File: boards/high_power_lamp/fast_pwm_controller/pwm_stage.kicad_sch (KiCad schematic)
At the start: 8 parts, among them Q1 BUK7516-55A,127, U1 4050

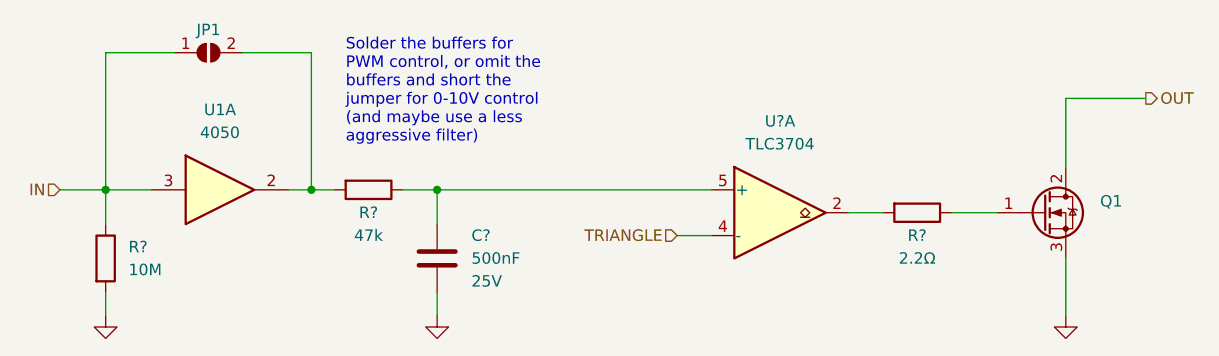
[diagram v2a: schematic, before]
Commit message: almost finish arranging the fast pwm controller pcb
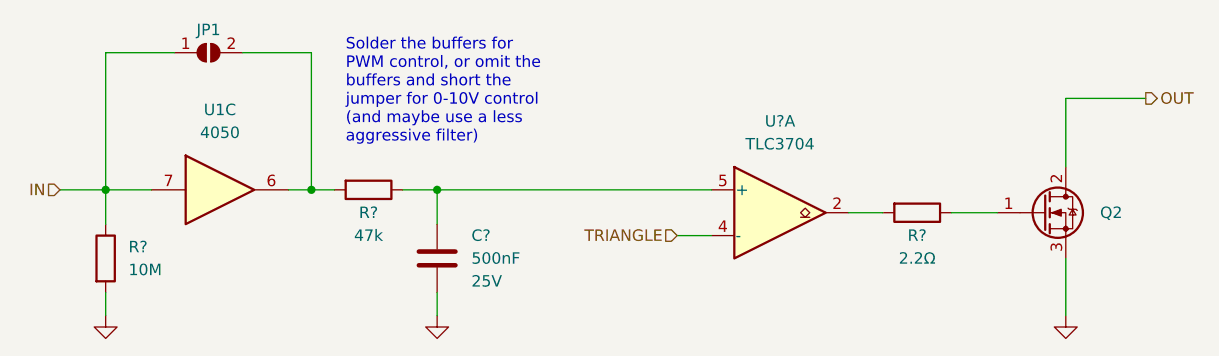
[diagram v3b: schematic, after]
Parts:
- renumbered Q1 to Q2
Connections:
- net IN: now also U1.7; no longer U1.3
- net at JP1.2 (B), R?.2: now also U1.6; no longer U1.2
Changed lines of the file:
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@@
         )
         (path "/ebb02bb0-15d4-41b5-b7b0-053d51d38d86/1dc02105-34f4-4dcd-909a-a43f3cf6326e"
+          (reference "R20") (unit 1)
+        )
+        (path "/ebb02bb0-15d4-41b5-b7b0-053d51d38d86/7bb7f3cd-bd16-48a2-9709-ee0db83f3451"
           (reference "R13") (unit 1)
-        )
-        (path "/ebb02bb0-15d4-41b5-b7b0-053d51d38d86/7bb7f3cd-bd16-48a2-9709-ee0db83f3451"
-          (reference "R20") (unit 1)
         )
         (path "/ebb02bb0-15d4-41b5-b7b0-053d51d38d86/abcbc788-820f-4167-8f5b-0037e0acabb5"
@@
     )
   )
-  (symbol (lib_id "4xxx:4050") (at 95.25 81.28 0) (unit 1)
+  (symbol (lib_id "4xxx:4050") (at 95.25 81.28 0) (unit 3)
     (in_bom yes) (on_board yes) (dnp no) (fields_autoplaced)
     (property "Reference" "U1" (at 95.25 72.39 0)
@@
       (project "fast_pwm_controller"
         (path "/ebb02bb0-15d4-41b5-b7b0-053d51d38d86/1dc02105-34f4-4dcd-909a-a43f3cf6326e"
+          (reference "U1") (unit 3)
+        )
+        (path "/ebb02bb0-15d4-41b5-b7b0-053d51d38d86/7bb7f3cd-bd16-48a2-9709-ee0db83f3451"
           (reference "U1") (unit 1)
         )
-        (path "/ebb02bb0-15d4-41b5-b7b0-053d51d38d86/7bb7f3cd-bd16-48a2-9709-ee0db83f3451"
+        (path "/ebb02bb0-15d4-41b5-b7b0-053d51d38d86/abcbc788-820f-4167-8f5b-0037e0acabb5"
+          (reference "U1") (unit 4)
+        )
+        (path "/ebb02bb0-15d4-41b5-b7b0-053d51d38d86/7c02a172-be14-404a-b556-b25540aed647"
           (reference "U1") (unit 2)
-        )
-        (path "/ebb02bb0-15d4-41b5-b7b0-053d51d38d86/abcbc788-820f-4167-8f5b-0037e0acabb5"
-          (reference "U1") (unit 3)
-        )
-        (path "/ebb02bb0-15d4-41b5-b7b0-053d51d38d86/7c02a172-be14-404a-b556-b25540aed647"
-          (reference "U1") (unit 4)
         )
       )
@@
   (symbol (lib_id "Device:Q_NMOS_GDS") (at 186.69 83.82 0) (unit 1)
     (in_bom yes) (on_board yes) (dnp no) (fields_autoplaced)
-    (property "Reference" "Q1" (at 193.04 82.55 0)
+    (property "Reference" "Q2" (at 193.04 83.82 0)
       (effects (font (size 1.27 1.27)) (justify left))
     )
@@
       (project "fast_pwm_controller"
         (path "/ebb02bb0-15d4-41b5-b7b0-053d51d38d86/1dc02105-34f4-4dcd-909a-a43f3cf6326e"
+          (reference "Q2") (unit 1)
+        )
+        (path "/ebb02bb0-15d4-41b5-b7b0-053d51d38d86/7bb7f3cd-bd16-48a2-9709-ee0db83f3451"
           (reference "Q1") (unit 1)
         )
-        (path "/ebb02bb0-15d4-41b5-b7b0-053d51d38d86/7bb7f3cd-bd16-48a2-9709-ee0db83f3451"
-          (reference "Q2") (unit 1)
-        )
-        (path "/ebb02bb0-15d4-41b5-b7b0-053d51d38d86/abcbc788-820f-4167-8f5b-0037e0acabb5"
+        (path "/ebb02bb0-15d4-41b5-b7b0-053d51d38d86/abcbc788-820f-4167-8f5b-0037e0acabb5"

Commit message: prepare traces
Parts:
- renumbered Q2 to Q1
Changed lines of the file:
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@@
         )
         (path "/ebb02bb0-15d4-41b5-b7b0-053d51d38d86/1dc02105-34f4-4dcd-909a-a43f3cf6326e"
-          (reference "#PWR034") (unit 1)
-        )
-        (path "/ebb02bb0-15d4-41b5-b7b0-053d51d38d86/7bb7f3cd-bd16-48a2-9709-ee0db83f3451"
-          (reference "#PWR047") (unit 1)
-        )
-        (path "/ebb02bb0-15d4-41b5-b7b0-053d51d38d86/abcbc788-820f-4167-8f5b-0037e0acabb5"
-          (reference "#PWR050") (unit 1)
-        )
-        (path "/ebb02bb0-15d4-41b5-b7b0-053d51d38d86/7c02a172-be14-404a-b556-b25540aed647"
-          (reference "#PWR053") (unit 1)
+          (reference "#PWR035") (unit 1)
+        )
+        (path "/ebb02bb0-15d4-41b5-b7b0-053d51d38d86/7bb7f3cd-bd16-48a2-9709-ee0db83f3451"
+          (reference "#PWR048") (unit 1)
+        )
+        (path "/ebb02bb0-15d4-41b5-b7b0-053d51d38d86/abcbc788-820f-4167-8f5b-0037e0acabb5"
+          (reference "#PWR051") (unit 1)
+        )
+        (path "/ebb02bb0-15d4-41b5-b7b0-053d51d38d86/7c02a172-be14-404a-b556-b25540aed647"
+          (reference "#PWR054") (unit 1)
         )
       )
@@
         )
         (path "/ebb02bb0-15d4-41b5-b7b0-053d51d38d86/1dc02105-34f4-4dcd-909a-a43f3cf6326e"
-          (reference "#PWR035") (unit 1)
-        )
-        (path "/ebb02bb0-15d4-41b5-b7b0-053d51d38d86/7bb7f3cd-bd16-48a2-9709-ee0db83f3451"
-          (reference "#PWR048") (unit 1)
-        )
-        (path "/ebb02bb0-15d4-41b5-b7b0-053d51d38d86/abcbc788-820f-4167-8f5b-0037e0acabb5"
-          (reference "#PWR051") (unit 1)
-        )
-        (path "/ebb02bb0-15d4-41b5-b7b0-053d51d38d86/7c02a172-be14-404a-b556-b25540aed647"
-          (reference "#PWR054") (unit 1)
+          (reference "#PWR036") (unit 1)
+        )
+        (path "/ebb02bb0-15d4-41b5-b7b0-053d51d38d86/7bb7f3cd-bd16-48a2-9709-ee0db83f3451"
+          (reference "#PWR049") (unit 1)
+        )
+        (path "/ebb02bb0-15d4-41b5-b7b0-053d51d38d86/abcbc788-820f-4167-8f5b-0037e0acabb5"
+          (reference "#PWR052") (unit 1)
+        )
+        (path "/ebb02bb0-15d4-41b5-b7b0-053d51d38d86/7c02a172-be14-404a-b556-b25540aed647"
+          (reference "#PWR055") (unit 1)
         )
       )
@@
         )
         (path "/ebb02bb0-15d4-41b5-b7b0-053d51d38d86/1dc02105-34f4-4dcd-909a-a43f3cf6326e"
+          (reference "R13") (unit 1)
+        )
+        (path "/ebb02bb0-15d4-41b5-b7b0-053d51d38d86/7bb7f3cd-bd16-48a2-9709-ee0db83f3451"
           (reference "R20") (unit 1)
-        )
-        (path "/ebb02bb0-15d4-41b5-b7b0-053d51d38d86/7bb7f3cd-bd16-48a2-9709-ee0db83f3451"
-          (reference "R13") (unit 1)
         )
         (path "/ebb02bb0-15d4-41b5-b7b0-053d51d38d86/abcbc788-820f-4167-8f5b-0037e0acabb5"
@@
         )
         (path "/ebb02bb0-15d4-41b5-b7b0-053d51d38d86/1dc02105-34f4-4dcd-909a-a43f3cf6326e"
-          (reference "#PWR036") (unit 1)
-        )
-        (path "/ebb02bb0-15d4-41b5-b7b0-053d51d38d86/7bb7f3cd-bd16-48a2-9709-ee0db83f3451"
-          (reference "#PWR049") (unit 1)
-        )
-        (path "/ebb02bb0-15d4-41b5-b7b0-053d51d38d86/abcbc788-820f-4167-8f5b-0037e0acabb5"
-          (reference "#PWR052") (unit 1)
-        )
-        (path "/ebb02bb0-15d4-41b5-b7b0-053d51d38d86/7c02a172-be14-404a-b556-b25540aed647"
-          (reference "#PWR055") (unit 1)
+          (reference "#PWR037") (unit 1)
+        )
+        (path "/ebb02bb0-15d4-41b5-b7b0-053d51d38d86/7bb7f3cd-bd16-48a2-9709-ee0db83f3451"
+          (reference "#PWR050") (unit 1)
+        )
+        (path "/ebb02bb0-15d4-41b5-b7b0-053d51d38d86/abcbc788-820f-4167-8f5b-0037e0acabb5"
+          (reference "#PWR053") (unit 1)
+        )
+        (path "/ebb02bb0-15d4-41b5-b7b0-053d51d38d86/7c02a172-be14-404a-b556-b25540aed647"
+          (reference "#PWR056") (unit 1)
         )
       )
@@
         )
         (path "/ebb02bb0-15d4-41b5-b7b0-053d51d38d86/1dc02105-34f4-4dcd-909a-a43f3cf6326e"
-          (reference "C7") (unit 1)
-        )
-        (path "/ebb02bb0-15d4-41b5-b7b0-053d51d38d86/7bb7f3cd-bd16-48a2-9709-ee0db83f3451"
-          (reference "C15") (unit 1)
-        )
-        (path "/ebb02bb0-15d4-41b5-b7b0-053d51d38d86/abcbc788-820f-4167-8f5b-0037e0acabb5"
+          (reference "C8") (unit 1)
+        )
+        (path "/ebb02bb0-15d4-41b5-b7b0-053d51d38d86/7bb7f3cd-bd16-48a2-9709-ee0db83f3451"
           (reference "C16") (unit 1)
         )
-        (path "/ebb02bb0-15d4-41b5-b7b0-053d51d38d86/7c02a172-be14-404a-b556-b25540aed647"
+        (path "/ebb02bb0-15d4-41b5-b7b0-053d51d38d86/abcbc788-820f-4167-8f5b-0037e0acabb5"
           (reference "C17") (unit 1)
+        )
+        (path "/ebb02bb0-15d4-41b5-b7b0-053d51d38d86/7c02a172-be14-404a-b556-b25540aed647"
+          (reference "C18") (unit 1)
         )
       )
@@
   (symbol (lib_id "Device:Q_NMOS_GDS") (at 186.69 83.82 0) (unit 1)
     (in_bom yes) (on_board yes) (dnp no) (fields_autoplaced)
-    (property "Reference" "Q2" (at 193.04 83.82 0)
+    (property "Reference" "Q1" (at 193.04 83.82 0)
       (effects (font (size 1.27 1.27)) (justify left))
     )
@@
       (project "fast_pwm_controller"
         (path "/ebb02bb0-15d4-41b5-b7b0-053d51d38d86/1dc02105-34f4-4dcd-909a-a43f3cf6326e"
+          (reference "Q1") (unit 1)
+        )
+        (path "/ebb02bb0-15d4-41b5-b7b0-053d51d38d86/7bb7f3cd-bd16-48a2-9709-ee0db83f3451"
           (reference "Q2") (unit 1)
         )
-        (path "/ebb02bb0-15d4-41b5-b7b0-053d51d38d86/7bb7f3cd-bd16-48a2-9709-ee0db83f3451"
-          (reference "Q1") (unit 1)
-        )
-        (path "/ebb02bb0-15d4-41b5-b7b0-053d51d38d86/abcbc788-820f-4167-8f5b-0037e0acabb5"
+        (path "/ebb02bb0-15d4-41b5-b7b0-053d51d38d86/abcbc788-820f-4167-8f5b-0037e0acabb5"

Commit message: arrange everything
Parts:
- gave numbers to parts that had none: 5
- renumbered Q1 to Q4
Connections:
- net TRIANGLE: now also U2.8 (-); no longer U2.4 (-)
- net at R26.2: now also U2.14; no longer U2.2
- net at C8.2, R12.1: now also U2.9 (+); no longer U2.5 (+)
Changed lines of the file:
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@@
   (symbol (lib_id "power:GND") (at 82.55 95.25 0) (unit 1)
     (in_bom yes) (on_board yes) (dnp no) (fields_autoplaced)
-    (property "Reference" "#PWR05" (at 82.55 101.6 0)
+    (property "Reference" "#PWR035" (at 82.55 101.6 0)
       (effects (font (size 1.27 1.27)) hide)
     )
@@
     (instances
       (project "fast_pwm_controller"
-        (path "/ebb02bb0-15d4-41b5-b7b0-053d51d38d86"
-          (reference "#PWR05") (unit 1)
-        )
-        (path "/ebb02bb0-15d4-41b5-b7b0-053d51d38d86/e05c2491-0151-410f-b890-9105113d0b96"
-          (reference "#PWR05") (unit 1)
-        )
         (path "/ebb02bb0-15d4-41b5-b7b0-053d51d38d86/1dc02105-34f4-4dcd-909a-a43f3cf6326e"
           (reference "#PWR035") (unit 1)
@@
     )
   )
-  (symbol (lib_id "Comparator:LM339") (at 157.48 83.82 0) (unit 1)
-    (in_bom yes) (on_board yes) (dnp no) (fields_autoplaced)
-    (property "Reference" "U?" (at 157.48 73.66 0)
+  (symbol (lib_id "Comparator:LM339") (at 157.48 83.82 0) (unit 4)
+    (in_bom yes) (on_board yes) (dnp no) (fields_autoplaced)
+    (property "Reference" "U2" (at 157.48 73.66 0)
       (effects (font (size 1.27 1.27)))
     )
@@
     (instances
       (project "fast_pwm_controller"
-        (path "/ebb02bb0-15d4-41b5-b7b0-053d51d38d86"
-          (reference "U?") (unit 1)
-        )
-        (path "/ebb02bb0-15d4-41b5-b7b0-053d51d38d86/1dc02105-34f4-4dcd-909a-a43f3cf6326e"
+        (path "/ebb02bb0-15d4-41b5-b7b0-053d51d38d86/1dc02105-34f4-4dcd-909a-a43f3cf6326e"
+          (reference "U2") (unit 4)
+        )
+        (path "/ebb02bb0-15d4-41b5-b7b0-053d51d38d86/7bb7f3cd-bd16-48a2-9709-ee0db83f3451"
+          (reference "U2") (unit 3)
+        )
+        (path "/ebb02bb0-15d4-41b5-b7b0-053d51d38d86/abcbc788-820f-4167-8f5b-0037e0acabb5"
+          (reference "U2") (unit 2)
+        )
+        (path "/ebb02bb0-15d4-41b5-b7b0-053d51d38d86/7c02a172-be14-404a-b556-b25540aed647"
           (reference "U2") (unit 1)
         )
-        (path "/ebb02bb0-15d4-41b5-b7b0-053d51d38d86/7bb7f3cd-bd16-48a2-9709-ee0db83f3451"
-          (reference "U2") (unit 2)
-        )
-        (path "/ebb02bb0-15d4-41b5-b7b0-053d51d38d86/abcbc788-820f-4167-8f5b-0037e0acabb5"
-          (reference "U2") (unit 3)
-        )
-        (path "/ebb02bb0-15d4-41b5-b7b0-053d51d38d86/7c02a172-be14-404a-b556-b25540aed647"
-          (reference "U2") (unit 4)
-        )
       )
     )
@@
   (symbol (lib_id "Device:R") (at 111.76 81.28 270) (unit 1)
     (in_bom yes) (on_board yes) (dnp no)
-    (property "Reference" "R?" (at 111.76 83.82 90)
+    (property "Reference" "R12" (at 111.76 83.82 90)
       (effects (font (size 1.27 1.27)))
     )
@@
     (instances
       (project "fast_pwm_controller"
-        (path "/ebb02bb0-15d4-41b5-b7b0-053d51d38d86"
-          (reference "R?") (unit 1)
-        )
-        (path "/ebb02bb0-15d4-41b5-b7b0-053d51d38d86/e05c2491-0151-410f-b890-9105113d0b96"
-          (reference "R?") (unit 1)
-        )
         (path "/ebb02bb0-15d4-41b5-b7b0-053d51d38d86/1dc02105-34f4-4dcd-909a-a43f3cf6326e"
           (reference "R12") (unit 1)
@@
   (symbol (lib_id "power:GND") (at 119.38 95.25 0) (unit 1)
     (in_bom yes) (on_board yes) (dnp no) (fields_autoplaced)
-    (property "Reference" "#PWR05" (at 119.38 101.6 0)
+    (property "Reference" "#PWR036" (at 119.38 101.6 0)
       (effects (font (size 1.27 1.27)) hide)
     )
@@
     (instances
       (project "fast_pwm_controller"
-        (path "/ebb02bb0-15d4-41b5-b7b0-053d51d38d86"
-          (reference "#PWR05") (unit 1)
-        )
-        (path "/ebb02bb0-15d4-41b5-b7b0-053d51d38d86/e05c2491-0151-410f-b890-9105113d0b96"
-          (reference "#PWR05") (unit 1)
-        )
         (path "/ebb02bb0-15d4-41b5-b7b0-053d51d38d86/1dc02105-34f4-4dcd-909a-a43f3cf6326e"
           (reference "#PWR036") (unit 1)
@@
   (symbol (lib_id "Device:R") (at 172.72 83.82 270) (unit 1)
     (in_bom yes) (on_board yes) (dnp no)
-    (property "Reference" "R?" (at 172.72 86.36 90)
+    (property "Reference" "R26" (at 172.72 86.36 90)
       (effects (font (size 1.27 1.27)))
     )
@@
     (instances
       (project "fast_pwm_controller"
-        (path "/ebb02bb0-15d4-41b5-b7b0-053d51d38d86"
-          (reference "R?") (unit 1)
-        )
-        (path "/ebb02bb0-15d4-41b5-b7b0-053d51d38d86/e05c2491-0151-410f-b890-9105113d0b96"
-          (reference "R?") (unit 1)
-        )
-        (path "/ebb02bb0-15d4-41b5-b7b0-053d51d38d86/1dc02105-34f4-4dcd-909a-a43f3cf6326e"
+        (path "/ebb02bb0-15d4-41b5-b7b0-053d51d38d86/1dc02105-34f4-4dcd-909a-a43f3cf6326e"
+          (reference "R26") (unit 1)
+        )
+        (path "/ebb02bb0-15d4-41b5-b7b0-053d51d38d86/7bb7f3cd-bd16-48a2-9709-ee0db83f3451"
+          (reference "R23") (unit 1)
+        )
+        (path "/ebb02bb0-15d4-41b5-b7b0-053d51d38d86/abcbc788-820f-4167-8f5b-0037e0acabb5"
           (reference "R13") (unit 1)
         )
-        (path "/ebb02bb0-15d4-41b5-b7b0-053d51d38d86/7bb7f3cd-bd16-48a2-9709-ee0db83f3451"
+        (path "/ebb02bb0-15d4-41b5-b7b0-053d51d38d86/7c02a172-be14-404a-b556-b25540aed647"
           (reference "R20") (unit 1)
         )
-        (path "/ebb02bb0-15d4-41b5-b7b0-053d51d38d86/abcbc788-820f-4167-8f5b-0037e0acabb5"
-          (reference "R23") (unit 1)
-        )
-        (path "/ebb02bb0-15d4-41b5-b7b0-053d51d38d86/7c02a172-be14-404a-b556-b25540aed647"
-          (reference "R26") (unit 1)
-        )
       )
     )
@@
   (symbol (lib_id "power:GND") (at 189.23 95.25 0) (unit 1)
     (in_bom yes) (on_board yes) (dnp no) (fields_autoplaced)
-    (property "Reference" "#PWR05" (at 189.23 101.6 0)
+    (property "Reference" "#PWR037" (at 189.23 101.6 0)
       (effects (font (size 1.27 1.27)) hide)
     )
@@
     (instances
       (project "fast_pwm_controller"
-        (path "/ebb02bb0-15d4-41b5-b7b0-053d51d38d86"
-          (reference "#PWR05") (unit 1)
-        )
-        (path "/ebb02bb0-15d4-41b5-b7b0-053d51d38d86/e05c2491-0151-410f-b890-9105113d0b96"
-          (reference "#PWR05") (unit 1)
-        )
         (path "/ebb02bb0-15d4-41b5-b7b0-053d51d38d86/1dc02105-34f4-4dcd-909a-a43f3cf6326e"
           (reference "#PWR037") (unit 1)
@@
   (symbol (lib_id "Device:C") (at 119.38 88.9 180) (unit 1)
     (in_bom yes) (on_board yes) (dnp no)
-    (property "Reference" "C?" (at 123.19 86.36 0)
+    (property "Reference" "C8" (at 123.19 86.36 0)
       (effects (font (size 1.27 1.27)) (justify right))
     )
@@
     (instances
       (project "fast_pwm_controller"
-        (path "/ebb02bb0-15d4-41b5-b7b0-053d51d38d86"
-          (reference "C?") (unit 1)
-        )
-        (path "/ebb02bb0-15d4-41b5-b7b0-053d51d38d86/e05c2491-0151-410f-b890-9105113d0b96"
-          (reference "C?") (unit 1)
-        )
         (path "/ebb02bb0-15d4-41b5-b7b0-053d51d38d86/1dc02105-34f4-4dcd-909a-a43f3cf6326e"
           (reference "C8") (unit 1)
@@
   (symbol (lib_id "Device:R") (at 82.55 88.9 0) (unit 1)
     (in_bom yes) (on_board yes) (dnp no)
-    (property "Reference" "R?" (at 85.09 87.63 0)
+    (property "Reference" "R11" (at 85.09 87.63 0)
       (effects (font (size 1.27 1.27)) (justify left))
     )
@@
     (instances
       (project "fast_pwm_controller"
-        (path "/ebb02bb0-15d4-41b5-b7b0-053d51d38d86"
-          (reference "R?") (unit 1)
-        )
-        (path "/ebb02bb0-15d4-41b5-b7b0-053d51d38d86/e05c2491-0151-410f-b890-9105113d0b96"
-          (reference "R?") (unit 1)
-        )
         (path "/ebb02bb0-15d4-41b5-b7b0-053d51d38d86/1dc02105-34f4-4dcd-909a-a43f3cf6326e"
           (reference "R11") (unit 1)
@@
   (symbol (lib_id "Device:Q_NMOS_GDS") (at 186.69 83.82 0) (unit 1)
     (in_bom yes) (on_board yes) (dnp no) (fields_autoplaced)
-    (property "Reference" "Q1" (at 193.04 83.82 0)
+    (property "Reference" "Q4" (at 193.04 83.82 0)
       (effects (font (size 1.27 1.27)) (justify left))
     )
@@
       (project "fast_pwm_controller"
         (path "/ebb02bb0-15d4-41b5-b7b0-053d51d38d86/1dc02105-34f4-4dcd-909a-a43f3cf6326e"
+          (reference "Q4") (unit 1)
+        )
+        (path "/ebb02bb0-15d4-41b5-b7b0-053d51d38d86/7bb7f3cd-bd16-48a2-9709-ee0db83f3451"
+          (reference "Q3") (unit 1)
+        )
+        (path "/ebb02bb0-15d4-41b5-b7b0-053d51d38d86/abcbc788-820f-4167-8f5b-0037e0acabb5"
           (reference "Q1") (unit 1)
         )
-        (path "/ebb02bb0-15d4-41b5-b7b0-053d51d38d86/7bb7f3cd-bd16-48a2-9709-ee0db83f3451"
+        (path "/ebb02bb0-15d4-41b5-b7b0-053d51d38d86/7c02a172-be14-404a-b556-b25540aed647"
           (reference "Q2") (unit 1)
         )
-        (path "/ebb02bb0-15d4-41b5-b7b0-053d51d38d86/abcbc788-820f-4167-8f5b-0037e0acabb5"
-          (reference "Q3") (unit 1)
-        )
-        (path "/ebb02bb0-15d4-41b5-b7b0-053d51d38d86/7c02a172-be14-404a-b556-b25540aed647"
-          (reference "Q4") (unit 1)
-        )
-      )
+      )
